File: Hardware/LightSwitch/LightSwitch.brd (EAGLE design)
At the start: 85.1 x 86 mm, 19 parts, among them IC1 ATMEGA328P, Q1 8MHz, X1 MAINS

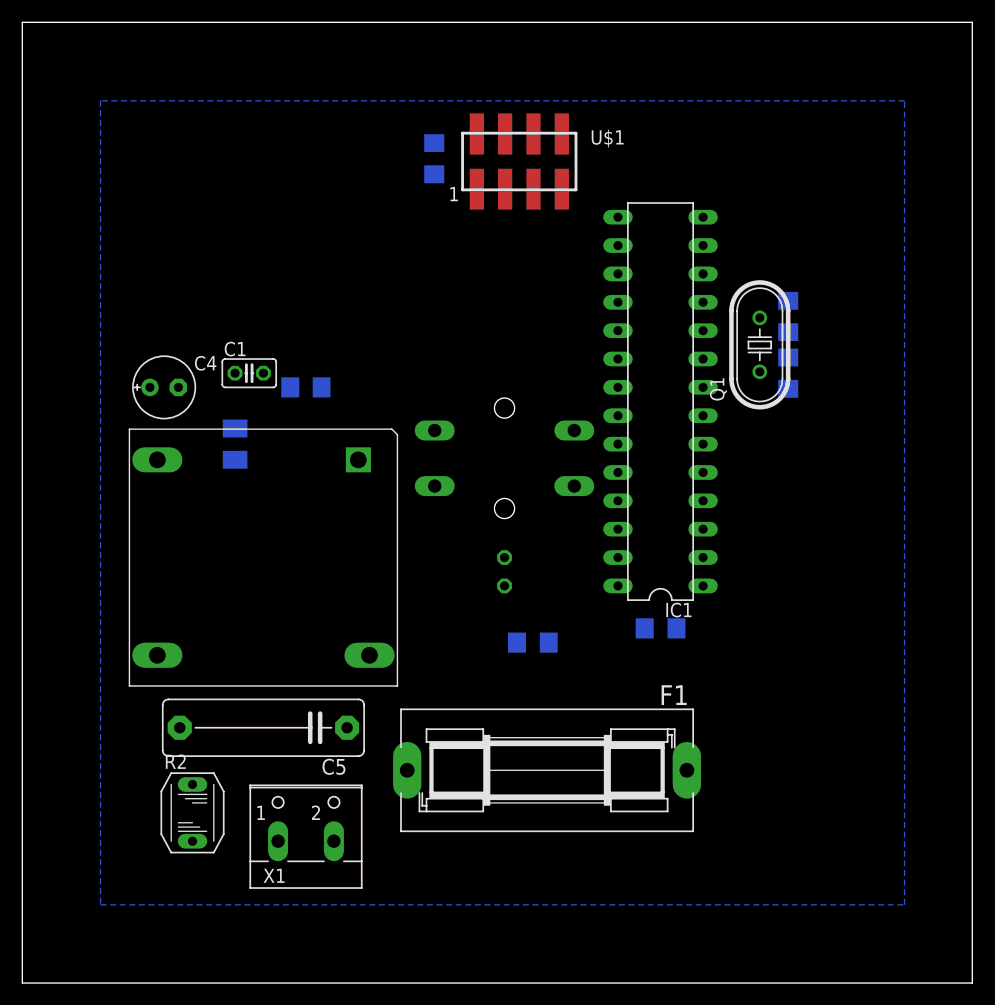
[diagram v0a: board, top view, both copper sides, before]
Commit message: updated schematic and created intial wired design for light switch
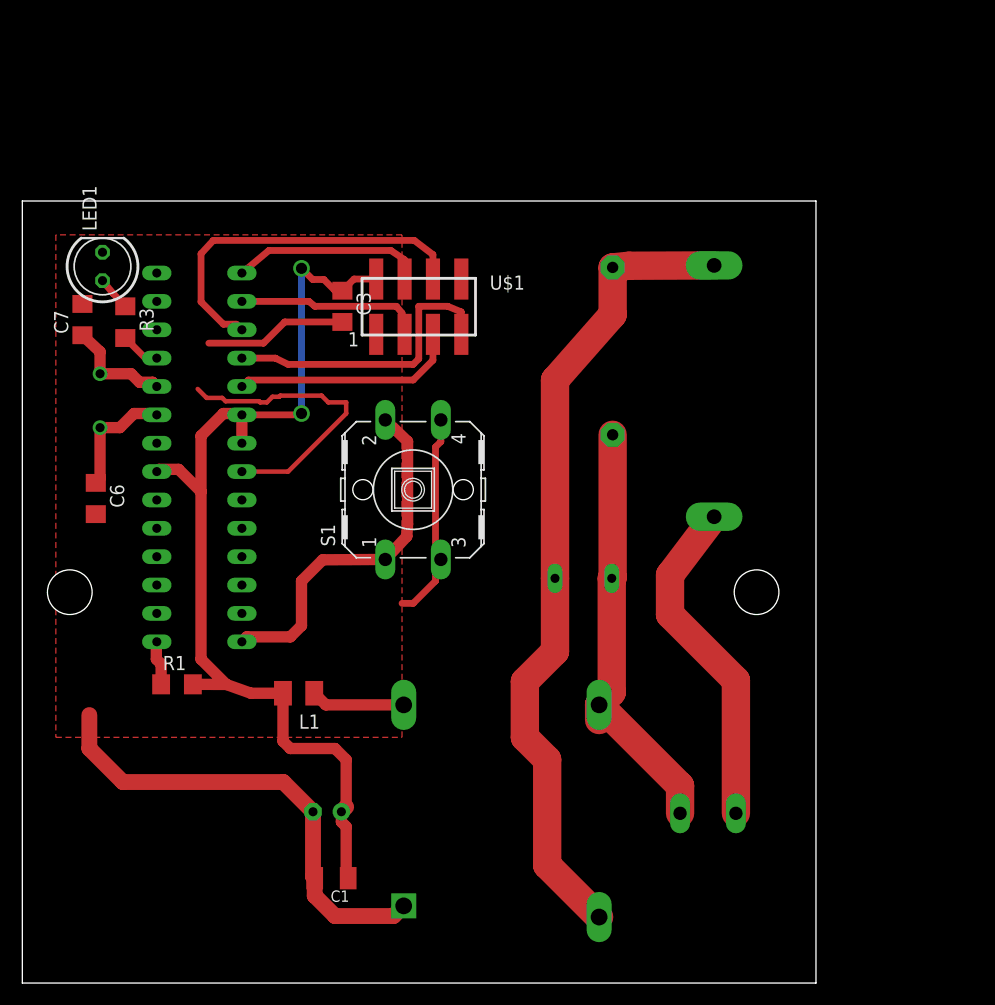
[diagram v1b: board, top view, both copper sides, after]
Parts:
- removed C2: 1u, rcl:C1206
- C1: device rcl:C025-025X050 -> rcl:C1206K
- F1: device fuse:SH25 -> fuse:SH22,5A
- moved C7 63.2 mm to (5.38, 59.4), flipped to the top, turned to 90 degrees
- moved C6 63.0 mm to (6.58, 43.4), flipped to the top, turned to 270 degrees
- moved Q1 59.3 mm to (6.96, 52.1), flipped to the bottom
- moved R3 46.4 mm to (9.22, 59.2), flipped to the top, turned to 270 degrees
- moved C5 46.0 mm to (52.9, 56.6), flipped to the bottom, turned to 270 degrees
- moved C1 45.8 mm to (27.7, 9.39), turned to 180 degrees
- moved LED1 45.2 mm to (7.18, 64.2), flipped to the top, turned to 90 degrees
- moved R1 43.6 mm to (13.8, 26.8), flipped to the top
- moved IC1 41.6 mm to (15.8, 47.1), flipped to the bottom
- moved R2 40.8 mm to (50.2, 36.2), flipped to the bottom, turned to 90 degrees
- moved C4 40.7 mm to (27.3, 15.3), flipped to the bottom
- moved F1 37.1 mm to (62.0, 53.0), flipped to the bottom, turned to 90 degrees
- moved X1 36.1 mm to (61.4, 16.5), flipped to the bottom
- moved U$2 31.1 mm to (42.9, 15.4), flipped to the bottom, turned to 0 degrees
- moved L1 23.0 mm to (24.7, 25.9), flipped to the top, turned to 180 degrees
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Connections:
- net +3V3: now also IC1.21; no longer C2.1
- net GND: no longer C2.2, IC1.21
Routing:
- net GND: track 0.00 -> 100.6 mm
- net +3V3: track 0.00 -> 91.4 mm, vias 0 -> 2
- net N$2: track 0.00 -> 73.1 mm
- net N$4: track 0.00 -> 38.8 mm
- net MOSI: track 0.00 -> 32.9 mm
- net N$7: track 0.00 -> 32.3 mm
- net N$1: track 0.00 -> 30.3 mm
- net MISO: track 0.00 -> 26.8 mm
- net SCK: track 0.00 -> 20.4 mm
- net CSN_RAD: track 0.00 -> 17.3 mm
- net CE_RAD: track 0.00 -> 16.8 mm
- net N$8: track 0.00 -> 10.8 mm
- net N$9: track 0.00 -> 9.69 mm
- net VOUT: track 0.00 -> 8.44 mm
- net N$3: track 0.00 -> 4.00 mm
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- added copper zone on layer 1, net GND
- removed copper zone on layer 16, net N$11
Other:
- board size 85.1 x 86 mm -> 71.1 x 70 mm

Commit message: updated incorrect outer dimension
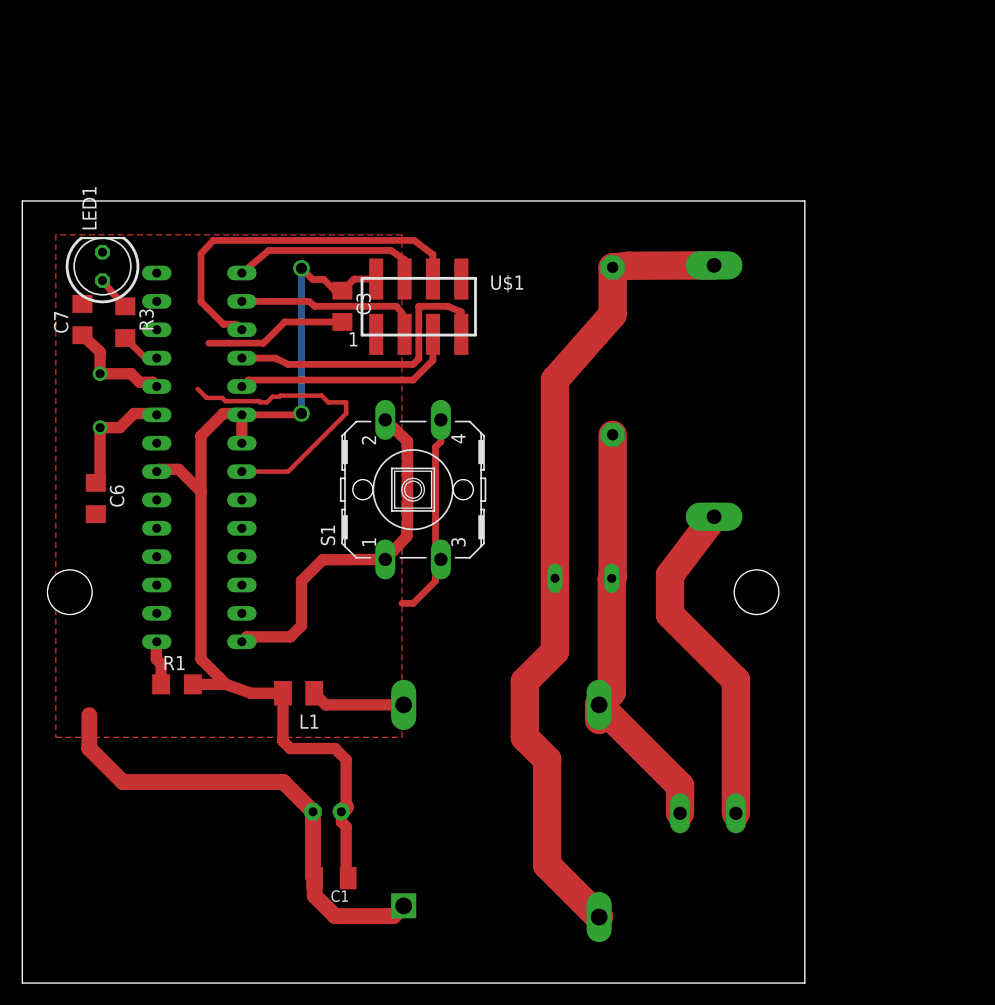
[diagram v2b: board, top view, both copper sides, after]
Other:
- board size 71.1 x 70 mm -> 70.1 x 70 mm
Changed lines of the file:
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@@
 <layer number="14" name="Route14" color="1" fill="6" visible="no" active="no"/>
 <layer number="15" name="Route15" color="4" fill="6" visible="no" active="no"/>
-<layer number="16" name="Bottom" color="1" fill="1" visible="no" active="yes"/>
+<layer number="16" name="Bottom" color="1" fill="1" visible="yes" active="yes"/>
 <layer number="17" name="Pads" color="2" fill="1" visible="yes" active="yes"/>
 <layer number="18" name="Vias" color="2" fill="1" visible="yes" active="yes"/>
@@
 <board>
 <plain>
-<wire x1="0" y1="0" x2="71.07" y2="0" width="0" layer="20"/>
-<wire x1="71.07" y1="0" x2="71.07" y2="70.03" width="0" layer="20"/>
-<wire x1="71.07" y1="70.03" x2="0" y2="70.03" width="0" layer="20"/>
+<wire x1="0" y1="0" x2="70.07" y2="0" width="0" layer="20"/>
+<wire x1="70.07" y1="0" x2="70.07" y2="70.03" width="0" layer="20"/>
+<wire x1="70.07" y1="70.03" x2="0" y2="70.03" width="0" layer="20"/>
 <wire x1="0" y1="70.03" x2="0" y2="0" width="0" layer="20"/>
 <hole x="4.25" y="35" drill="4"/>
